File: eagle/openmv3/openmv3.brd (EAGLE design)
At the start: 35.6 x 45.7 mm, 64 parts, among them J3 CON_HEADER_1X03, J4 CON_HEADER_1X03, Q1 MOSFET, U12 STM32F407LQFP100, U2 USD-47571, U4 TPS768, U8 VREG_25, U9 OV2640, X2 USB-MICROB

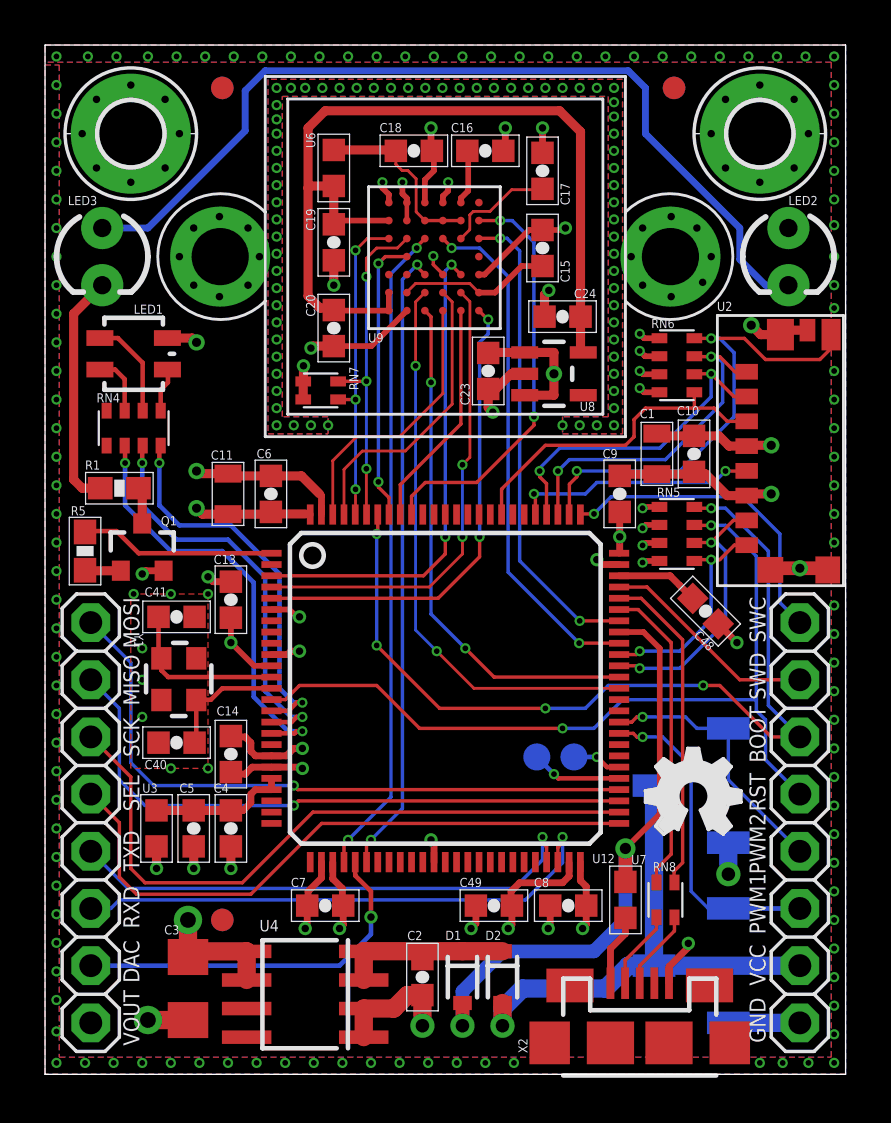
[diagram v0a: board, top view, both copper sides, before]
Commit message: Update HW
* Connect STROBE, FREX and EXPST_B
* Remove shield.
* Add pull-down to IR MOSFET
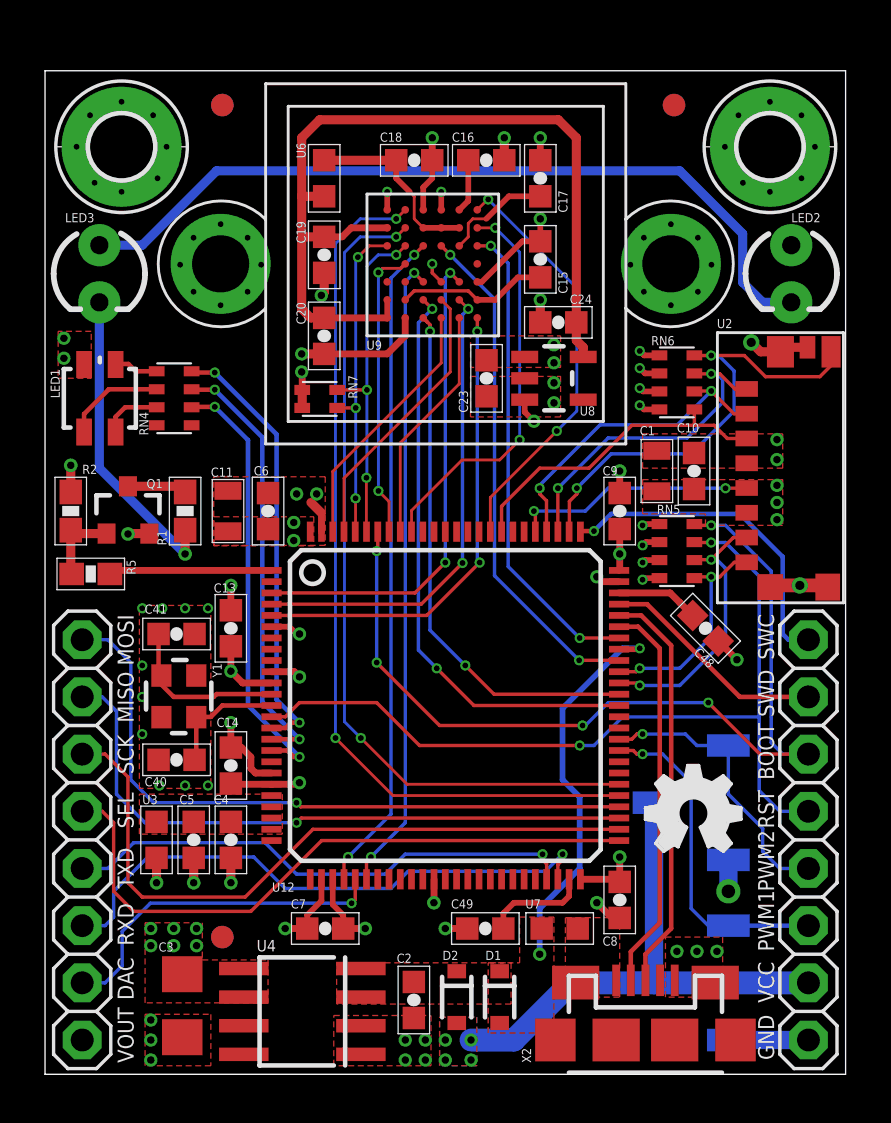
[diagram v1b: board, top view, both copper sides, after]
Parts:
- removed RN8: 27R, resistor-dil:EXBV4V
- removed TP1, TP2: TPTP12R, testpad:TP12R
- added R2: 10k, sfe:0603-RES
- moved U7 3.19 mm to (22.9, 6.48), turned to 180 degrees
- moved R1 3.09 mm to (6.22, 25.0), turned to 270 degrees
- moved LED1 2.48 mm to (2.43, 30.0), turned to 180 degrees
- moved C8 2.30 mm to (25.5, 7.75), turned to 270 degrees
- moved RN4 2.24 mm to (5.74, 30.0), turned to 270 degrees
- moved D2 2.22 mm to (18.3, 3.43)
- moved D1 1.88 mm to (20.2, 3.43)
- moved Q1 1.77 mm to (3.68, 25.0)
- moved C13 1.27 mm to (8.26, 19.8)
- moved C49 1.09 mm to (19.6, 6.48)
- moved C2 1.09 mm to (16.4, 3.30)
- moved R5 1.05 mm to (2.03, 22.2), turned to 180 degrees
- moved C7 1.02 mm to (12.4, 6.48)
- moved JP3 0.85 mm to (33.9, 10.4)
- moved JP4 0.85 mm to (1.65, 10.4)
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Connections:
- removed net N$15: RN8.3, X2.D-
- removed net N$17: RN8.4, X2.D+
- removed net N$19: TP1.TP, U12.55
- removed net N$20: TP2.TP, U12.56
- new net EXPST: U12.55, U9.A2
- new net FREX: U12.56, U9.B2
- new net STROBE: U12.84, U9.A6
- net FS_DM: now also X2.D-; no longer RN8.2
- net FS_DP: now also X2.D+; no longer RN8.1
- net GND: now also R2.1; no longer H2.B2,8, H6.B2,8, U$1.P$1, U$1.P$2, U9.A2, U9.B2
- net N$5: now also R2.2
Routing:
- net EXPST: track 0.00 -> 39.3 mm, vias 0 -> 2
- net FREX: track 0.00 -> 37.3 mm, vias 0 -> 2
- net GND: track 77.2 -> 52.8 mm, vias 255 -> 55
- net VCC: track 49.2 -> 26.3 mm, vias 20 -> 30
- net STROBE: track 0.00 -> 18.7 mm, vias 0 -> 2
- net VBUS: track 27.4 -> 17.4 mm
- net VIN: track 7.89 -> 0.00 mm
- net N$12: track 6.21 -> 0.00 mm
- net N$16: track 40.4 -> 35.8 mm
- net N$19: track 4.05 -> 0.00 mm
- net FS_DP: track 14.5 -> 18.2 mm
- net FS_DM: track 13.8 -> 17.5 mm
- net N$17: track 3.56 -> 0.00 mm, vias 0 -> 1
- net N$15: track 3.50 -> 0.00 mm, vias 0 -> 1
- net N$10: track 10.5 -> 13.8 mm, vias 0 -> 1
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- added copper zone on layer 1, net N$12
- added copper zone on layer 1, net N$7
- added copper zone on layer 1, net RAW
- added copper zone on layer 16, net RAW
- added copper zone on layer 1, net VBUS
- added copper zone on layer 1, net VCC
- added copper zone on layer 1, net VIN
- removed copper zone on layer 16, net GND
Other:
- board size 35.6 x 45.7 mm -> 35.6 x 44.6 mm

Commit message: Add shields and update OMV3
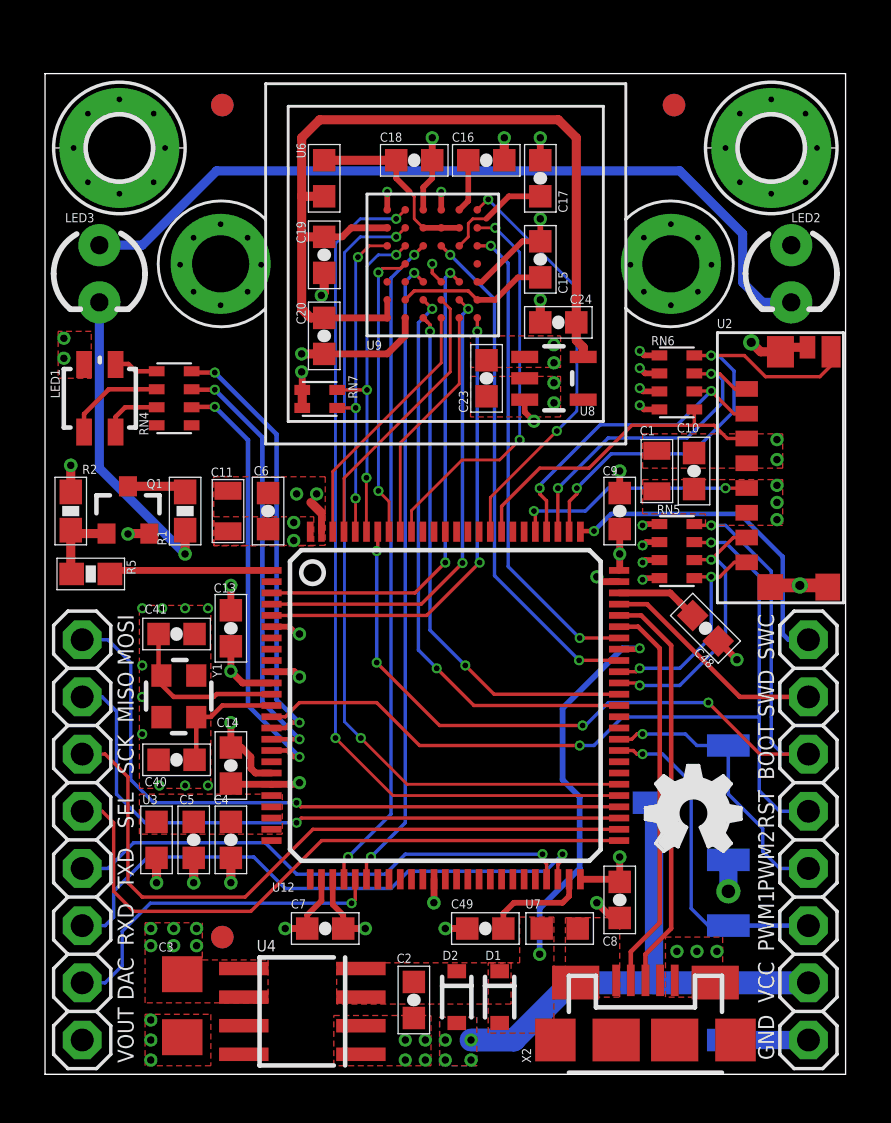
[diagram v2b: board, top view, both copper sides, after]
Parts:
- moved H2 0.11 mm to (3.30, 41.1)
- moved H6 0.08 mm to (32.3, 41.1)
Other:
- board size 35.6 x 44.6 mm -> 35.6 x 44.5 mm
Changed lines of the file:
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@@
 <layer number="47" name="Measures" color="7" fill="1" visible="no" active="yes"/>
 <layer number="48" name="Document" color="7" fill="1" visible="no" active="yes"/>
-<layer number="49" name="Reference" color="7" fill="1" visible="no" active="yes"/>
+<layer number="49" name="Reference" color="7" fill="1" visible="yes" active="yes"/>
 <layer number="50" name="dxf" color="7" fill="1" visible="no" active="no"/>
 <layer number="51" name="tDocu" color="7" fill="1" visible="no" active="yes"/>
@@
 <layer number="147" name="mMeasures" color="7" fill="1" visible="no" active="yes"/>
 <layer number="148" name="mDocument" color="7" fill="1" visible="no" active="yes"/>
-<layer number="149" name="mReference" color="7" fill="1" visible="no" active="yes"/>
+<layer number="149" name="mReference" color="7" fill="1" visible="yes" active="yes"/>
 <layer number="150" name="Notes" color="7" fill="1" visible="no" active="yes"/>
 <layer number="151" name="HeatSink" color="7" fill="1" visible="no" active="yes"/>
@@
 <board>
 <plain>
-<wire x1="0" y1="44.577" x2="0" y2="0" width="0" layer="20"/>
+<wire x1="0" y1="44.45" x2="0" y2="0" width="0" layer="20"/>
 <wire x1="0" y1="0" x2="35.56" y2="0" width="0" layer="20"/>
-<wire x1="35.56" y1="0" x2="35.56" y2="44.577" width="0" layer="20"/>
-<wire x1="35.56" y1="44.577" x2="0" y2="44.577" width="0" layer="20"/>
+<wire x1="35.56" y1="0" x2="35.56" y2="44.45" width="0" layer="20"/>
+<wire x1="35.56" y1="44.45" x2="0" y2="44.45" width="0" layer="20"/>
 <text x="3.937" y="3.302" size="0.7112" layer="21" font="vector" ratio="20" rot="R90">DAC</text>
 <text x="3.937" y="8.255" size="0.7112" layer="21" font="vector" ratio="20" rot="R90">TXD</text>
@@
 </autorouter>
 <elements>
-<element name="H6" library="holes" package="2,8-PAD" value="MOUNT-PAD-ROUND2.8" x="32.2" y="41.2" smashed="yes" rot="R270"/>
+<element name="H6" library="holes" package="2,8-PAD" value="MOUNT-PAD-ROUND2.8" x="32.258" y="41.148" smashed="yes" rot="R270"/>
 <element name="C40" library="sfe" package="0603-CAP" value="12pF" x="5.842" y="13.97" smashed="yes">
 <attribute name="NAME" x="4.4232125" y="12.7943125" size="0.4064" layer="25" font="vector" ratio="20"/>
@@
 </element>
 <element name="U$1" library="omnivision" package="LENSMOUNT-20MM" value="LENSMOUNT20MM" x="17.8" y="36" smashed="yes"/>
-<element name="H2" library="holes" package="2,8-PAD" value="MOUNT-PAD-ROUND2.8" x="3.4" y="41.2" smashed="yes" rot="R90"/>
+<element name="H2" library="holes" package="2,8-PAD" value="MOUNT-PAD-ROUND2.8" x="3.302" y="41.148" smashed="yes" rot="R90"/>
 <element name="RN6" library="resistor-dil" package="EXBV8V" value="10K" x="28.067" y="30.734" smashed="yes" rot="R270">
 <attribute name="OC_NEWARK" value="unknown" x="28.067" y="30.734" size="1.778" layer="27" rot="R270" display="off"/>
@@
 </signal>
 <signal name="N$34">
-<via x="3.4" y="43.2" extent="1-16" drill="0.254"/>
+<via x="3.302" y="43.307" extent="1-16" drill="0.254"/>
 </signal>
 <signal name="N$35">
-<via x="3.4" y="39.2" extent="1-16" drill="0.254"/>
+<via x="3.302" y="39.116" extent="1-16" drill="0.254"/>
 </signal>
 <signal name="N$36">
-<via x="5.4" y="41.2" extent="1-16" drill="0.254"/>
+<via x="5.334" y="41.148" extent="1-16" drill="0.254"/>
 </signal>
 <signal name="N$37">
-<via x="1.4" y="41.2" extent="1-16" drill="0.254"/>
+<via x="1.27" y="41.148" extent="1-16" drill="0.254"/>
 </signal>
 <signal name="N$38">
-<via x="2.2" y="39.6" extent="1-16" drill="0.254"/>
+<via x="1.905" y="39.624" extent="1-16" drill="0.254"/>
 </signal>
 <signal name="N$39">
-<via x="5" y="39.8" extent="1-16" drill="0.254"/>
+<via x="4.826" y="39.624" extent="1-16" drill="0.254"/>
 </signal>
 <signal name="N$40">
-<via x="2" y="42.6" extent="1-16" drill="0.254"/>
+<via x="1.905" y="42.672" extent="1-16" drill="0.254"/>
 </signal>
 <signal name="N$41">
-<via x="4.8" y="42.6" extent="1-16" drill="0.254"/>
+<via x="4.826" y="42.672" extent="1-16" drill="0.254"/>
 </signal>
 <signal name="N$42">
-<via x="32.2" y="43.2" extent="1-16" drill="0.254"/>
+<via x="32.258" y="43.307" extent="1-16" drill="0.254"/>
 </signal>
 <signal name="N$43">
-<via x="34.2" y="41.2" extent="1-16" drill="0.254"/>
+<via x="34.29" y="41.148" extent="1-16" drill="0.254"/>
 </signal>
 <signal name="N$44">
-<via x="32.2" y="39.2" extent="1-16" drill="0.254"/>
+<via x="32.258" y="39.116" extent="1-16" drill="0.254"/>
 </signal>
 <signal name="N$45">
-<via x="30.2" y="41.2" extent="1-16" drill="0.254"/>
+<via x="30.226" y="41.148" extent="1-16" drill="0.254"/>
 </signal>
 <signal name="N$46">
-<via x="33.6" y="42.6" extent="1-16" drill="0.254"/>
+<via x="33.782" y="42.672" extent="1-16" drill="0.254"/>
 </signal>
 <signal name="N$47">
-<via x="30.8" y="42.6" extent="1-16" drill="0.254"/>
+<via x="30.861" y="42.672" extent="1-16" drill="0.254"/>
 </signal>
 <signal name="N$48">
-<via x="33.6" y="39.8" extent="1-16" drill="0.254"/>
+<via x="33.782" y="39.624" extent="1-16" drill="0.254"/>
 </signal>
 <signal name="N$49">
-<via x="31" y="39.6" extent="1-16" drill="0.254"/>
+<via x="30.861" y="39.624" extent="1-16" drill="0.254"/>
 </signal>
 </signals>
-<errors>
-</errors>
 </board>
 </drawing>

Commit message: Update design files
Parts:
- added U$3: (no value), openmv:OMV-LOGO
- C2: value 4.7 -> 4.7uF
- C23, C24: value 1uF -> 4.7uF
- U8: value VREG_25 -> VREG_28
- moved LOGO1 1.55 mm to (26.9, 11.4)
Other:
- board text removed: "penMV"
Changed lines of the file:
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@@
 <layer number="47" name="Measures" color="7" fill="1" visible="no" active="yes"/>
 <layer number="48" name="Document" color="7" fill="1" visible="no" active="yes"/>
-<layer number="49" name="Reference" color="7" fill="1" visible="yes" active="yes"/>
+<layer number="49" name="Reference" color="7" fill="1" visible="no" active="yes"/>
 <layer number="50" name="dxf" color="7" fill="1" visible="no" active="no"/>
 <layer number="51" name="tDocu" color="7" fill="1" visible="no" active="yes"/>
@@
 <layer number="147" name="mMeasures" color="7" fill="1" visible="no" active="yes"/>
 <layer number="148" name="mDocument" color="7" fill="1" visible="no" active="yes"/>
-<layer number="149" name="mReference" color="7" fill="1" visible="yes" active="yes"/>
+<layer number="149" name="mReference" color="7" fill="1" visible="no" active="yes"/>
 <layer number="150" name="Notes" color="7" fill="1" visible="no" active="yes"/>
 <layer number="151" name="HeatSink" color="7" fill="1" visible="no" active="yes"/>
@@
 <text x="3.937" y="13.335" size="0.7112" layer="21" font="vector" ratio="20" rot="R90">SCK</text>
 <text x="3.937" y="15.621" size="0.7112" layer="21" font="vector" ratio="20" rot="R90">MISO</text>
-<wire x1="14.986" y1="2.413" x2="14.986" y2="1.143" width="0.127" layer="22"/>
-<wire x1="14.986" y1="1.143" x2="13.716" y2="1.143" width="0.127" layer="22"/>
-<wire x1="13.716" y1="1.143" x2="13.716" y2="2.413" width="0.127" layer="22"/>
-<wire x1="13.716" y1="2.413" x2="14.986" y2="2.413" width="0.127" layer="22"/>
-<circle x="14.732" y="2.159" radius="0.0508" width="0.1016" layer="22"/>
-<circle x="14.351" y="2.159" radius="0.0508" width="0.1016" layer="22"/>
-<circle x="13.97" y="2.159" radius="0.0508" width="0.1016" layer="22"/>
-<circle x="13.97" y="1.778" radius="0.0508" width="0.1016" layer="22"/>
-<circle x="14.351" y="1.778" radius="0.0508" width="0.1016" layer="22"/>
-<circle x="14.732" y="1.778" radius="0.0508" width="0.1016" layer="22"/>
-<circle x="14.732" y="1.397" radius="0.0508" width="0.1016" layer="22"/>
-<circle x="14.351" y="1.397" radius="0.0508" width="0.1016" layer="22"/>
-<circle x="13.97" y="1.397" radius="0.0508" width="0.1016" layer="22"/>
-<circle x="14.351" y="1.778" radius="1.27" width="0.254" layer="22"/>
-<text x="12.827" y="0.635" size="1.6764" layer="22" font="vector" ratio="17" rot="MR0">penMV</text>
 <text x="32.385" y="15.875" size="0.7112" layer="21" font="vector" ratio="20" rot="R90">SWD</text>
 <text x="32.385" y="18.415" size="0.7112" layer="21" font="vector" ratio="20" rot="R90">SWC</text>
@@
 <attribute name="VALUE" x="11.257" y="33.8795" size="0.4064" layer="27" rot="R270"/>
 </element>
-<element name="C23" library="sfe" package="0603-CAP" value="1uF" x="19.612" y="30.915" smashed="yes" rot="R270">
+<element name="C23" library="sfe" package="0603-CAP" value="4.7uF" x="19.612" y="30.915" smashed="yes" rot="R270">
 <attribute name="NAME" x="18.7865" y="29.391" size="0.4064" layer="25" font="vector" ratio="20" rot="R90"/>
 <attribute name="VALUE" x="18.215" y="31.931" size="0.4064" layer="27" rot="R270"/>
 </element>
-<element name="C24" library="sfe" package="0603-CAP" value="1uF" x="22.8" y="33.4" smashed="yes" rot="R180">
+<element name="C24" library="sfe" package="0603-CAP" value="4.7uF" x="22.8" y="33.4" smashed="yes" rot="R180">
 <attribute name="NAME" x="23.308" y="34.2255" size="0.4064" layer="25" font="vector" ratio="20"/>
 <attribute name="VALUE" x="23.816" y="34.797" size="0.4064" layer="27" rot="R180"/>
 </element>
-<element name="U8" library="sfe" package="SOT23-5" value="VREG_25" x="22.606" y="30.915" smashed="yes" rot="R270">
+<element name="U8" library="sfe" package="SOT23-5" value="VREG_28" x="22.606" y="30.915" smashed="yes" rot="R270">
 <attribute name="NAME" x="23.749" y="29.264" size="0.4064" layer="25" font="vector" ratio="20"/>
 <attribute name="VALUE" x="22.4155" y="31.8675" size="0.4064" layer="27" rot="R270"/>
@@
 <attribute name="VALUE" x="3.693" y="16.74200625" size="0.4064" layer="25" rot="SR270"/>
 </element>
-<element name="LOGO1" library="iofault" package="OSHW_FILLX150_NOTEXT" value="OSHW_LOGO_FILLX0150-NT" x="26.67" y="9.906" smashed="yes"/>
+<element name="LOGO1" library="iofault" package="OSHW_FILLX150_NOTEXT" value="OSHW_LOGO_FILLX0150-NT" x="26.924" y="11.43" smashed="yes"/>
 <element name="U12" library="mux" package="LQFP100" value="STM32F407LQFP100" x="17.78" y="16.383" smashed="yes">
 <attribute name="NAME" x="10.081" y="8.112" size="0.4064" layer="25" font="vector" ratio="20"/>
@@
 <attribute name="VALUE" x="5.08" y="26.0985" size="0.4064" layer="27" rot="R270"/>
 </element>
-<element name="C2" library="sfe" package="0603-CAP" value="4.7" x="16.383" y="3.302" smashed="yes" rot="R270">
+<element name="C2" library="sfe" package="0603-CAP" value="4.7uF" x="16.383" y="3.302" smashed="yes" rot="R270">
 <attribute name="NAME" x="15.621" y="4.953" size="0.4064" layer="25" font="vector" ratio="20"/>
 <attribute name="VALUE" x="15.683" y="4.202" size="0.4064" layer="27" rot="R270"/>
@@
 <attribute name="VALUE" x="0" y="26.035" size="0.4064" layer="27" font="vector" rot="R270"/>
 </element>
+<element name="U$3" library="openmv" package="OMV-LOGO" value="" x="17.526" y="1.524" rot="MR0"/>
 </elements>
 <signals>
